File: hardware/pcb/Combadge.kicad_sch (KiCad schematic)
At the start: 12 parts, among them J1 Conn_01x05_Female, U2 ESP32-WROOM-32

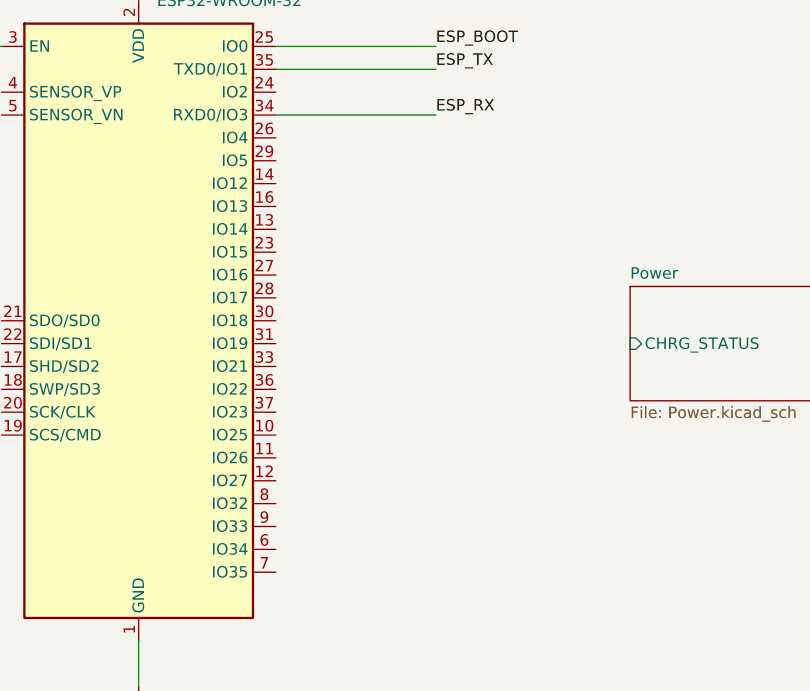
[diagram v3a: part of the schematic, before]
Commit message: Connect I2S devices to ESP32
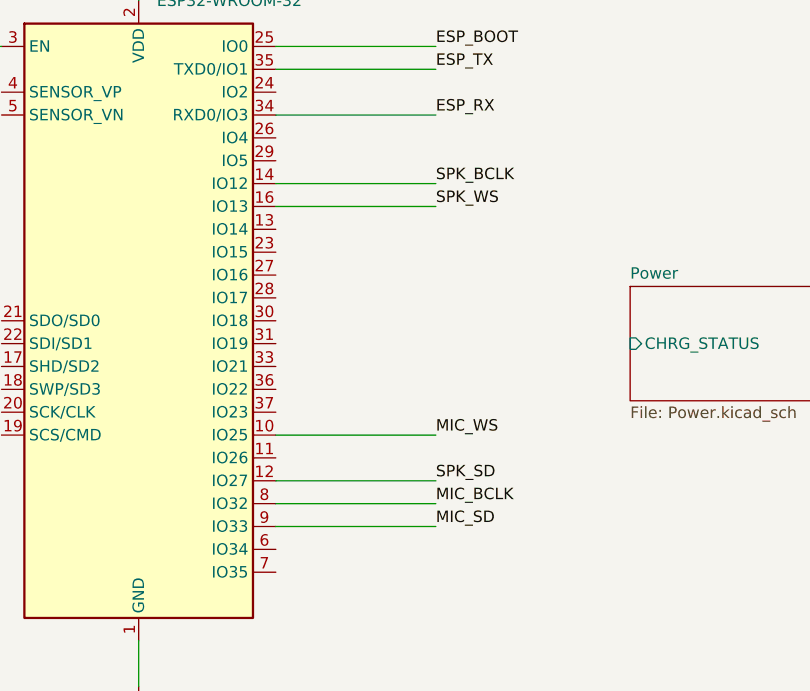
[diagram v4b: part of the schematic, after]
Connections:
- net MIC_BCLK: now also U2.8 (IO32)
- net MIC_SD: now also U2.9 (IO33)
- net MIC_WS: now also U2.10 (IO25)
- net SPK_BCLK: now also U2.14 (IO12)
- net SPK_SD: now also U2.12 (IO27)
- net SPK_WS: now also U2.16 (IO13)
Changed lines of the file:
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@@
+    (stroke (width 0) (type default) (color 0 0 0 0))
+  )
+  (wire (pts (xy 88.9 71.12) (xy 106.68 71.12))
     (stroke (width 0) (type default) (color 0 0 0 0))
   )
@@
     (stroke (width 0) (type default) (color 0 0 0 0))
   )
+  (wire (pts (xy 88.9 109.22) (xy 106.68 109.22))
+    (stroke (width 0) (type default) (color 0 0 0 0))
+  )
   (wire (pts (xy 88.9 63.5) (xy 106.68 63.5))
     (stroke (width 0) (type default) (color 0 0 0 0))
@@
     (stroke (width 0) (type default) (color 0 0 0 0))
   )
+  (wire (pts (xy 88.9 104.14) (xy 106.68 104.14))
+    (stroke (width 0) (type default) (color 0 0 0 0))
+  )
   (wire (pts (xy 20.32 181.61) (xy 34.29 181.61))
     (stroke (width 0) (type default) (color 0 0 0 0))
@@
     (stroke (width 0) (type default) (color 0 0 0 0))
   )
+  (wire (pts (xy 88.9 106.68) (xy 106.68 106.68))
+    (stroke (width 0) (type default) (color 0 0 0 0))
+  )
+  (wire (pts (xy 88.9 99.06) (xy 106.68 99.06))
+    (stroke (width 0) (type default) (color 0 0 0 0))
+  )
   (wire (pts (xy 77.47 31.75) (xy 73.66 31.75))
     (stroke (width 0) (type default) (color 0 0 0 0))
@@
     (stroke (width 0) (type default) (color 0 0 0 0))
   )
+  (wire (pts (xy 88.9 73.66) (xy 106.68 73.66))
+    (stroke (width 0) (type default) (color 0 0 0 0))
+  )
   (text "No clip gain mode" (at 261.62 110.49 0)
     (effects (font (size 1.27 1.27)) (justify left bottom))
@@
     (effects (font (size 1.27 1.27)) (justify left bottom))
   )
+  (label "SPK_BCLK" (at 106.68 71.12 0)
+    (effects (font (size 1.27 1.27)) (justify left bottom))
+  )
   (label "SPK_EN" (at 212.09 92.71 0)
     (effects (font (size 1.27 1.27)) (justify left bottom))
@@
     (effects (font (size 1.27 1.27)) (justify left bottom))
   )
+  (label "SPK_WS" (at 106.68 73.66 0)
+    (effects (font (size 1.27 1.27)) (justify left bottom))
+  )
+  (label "MIC_BCLK" (at 106.68 106.68 0)
+    (effects (font (size 1.27 1.27)) (justify left bottom))
+  )
   (label "ESP_TX" (at 106.68 58.42 0)
     (effects (font (size 1.27 1.27)) (justify left bottom))
   )
+  (label "MIC_SD" (at 106.68 109.22 0)
+    (effects (font (size 1.27 1.27)) (justify left bottom))
+  )
+  (label "MIC_WS" (at 106.68 99.06 0)
+    (effects (font (size 1.27 1.27)) (justify left bottom))
+  )
   (label "SPK_WS" (at 264.16 90.17 0)
     (effects (font (size 1.27 1.27)) (justify left bottom))
   )
+  (label "SPK_SD" (at 106.68 104.14 0)
+    (effects (font (size 1.27 1.27)) (justify left bottom))
+  )

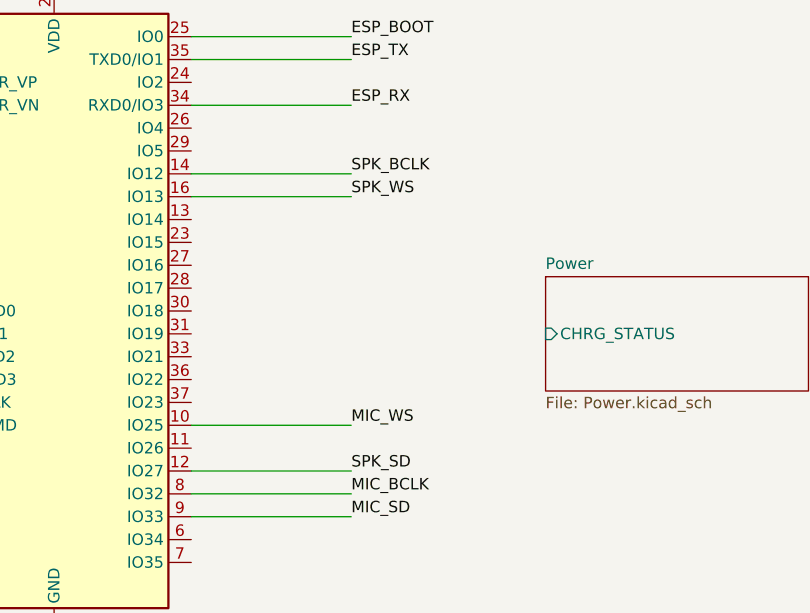
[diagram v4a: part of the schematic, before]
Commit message: Make ancillary ESP32 connections
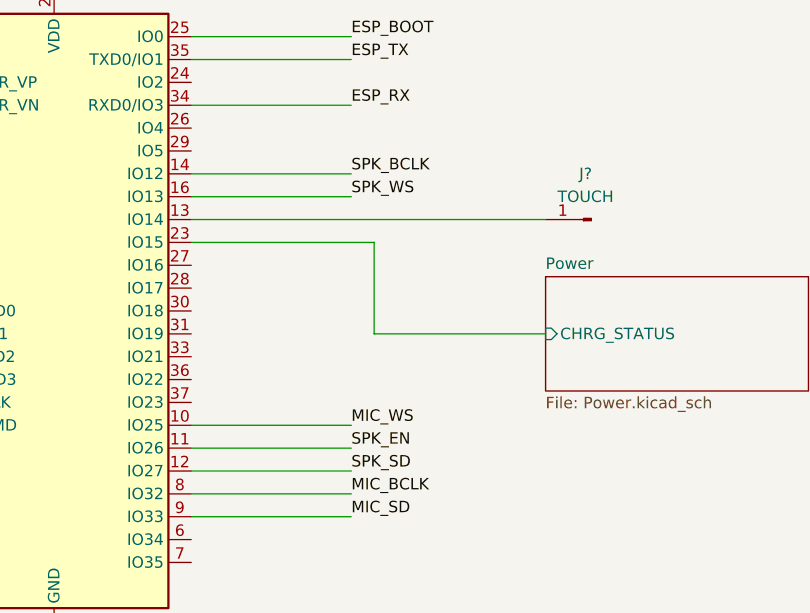
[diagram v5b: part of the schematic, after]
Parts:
- added J?: TOUCH, symbol Connector:Conn_01x01_Male
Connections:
- net Power/CHRG_STATUS: now also U2.23 (IO15)
- net SPK_EN: now also U2.11 (IO26)
- net at U2.13 (IO14): now also J?.1 (Pin_1)
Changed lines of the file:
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@@
+    (stroke (width 0) (type default) (color 0 0 0 0))
+  )
+  (wire (pts (xy 109.22 88.9) (xy 128.27 88.9))
     (stroke (width 0) (type default) (color 0 0 0 0))
   )
@@
     (stroke (width 0) (type default) (color 0 0 0 0))
   )
+  (wire (pts (xy 109.22 78.74) (xy 109.22 88.9))
+    (stroke (width 0) (type default) (color 0 0 0 0))
+  )
   (wire (pts (xy 220.98 87.63) (xy 228.6 87.63))
     (stroke (width 0) (type default) (color 0 0 0 0))
@@
     (stroke (width 0) (type default) (color 0 0 0 0))
   )
+  (wire (pts (xy 88.9 101.6) (xy 106.68 101.6))
+    (stroke (width 0) (type default) (color 0 0 0 0))
+  )
   (wire (pts (xy 248.92 29.21) (xy 256.54 29.21))
     (stroke (width 0) (type default) (color 0 0 0 0))
@@
     (stroke (width 0) (type default) (color 0 0 0 0))
   )
+  (wire (pts (xy 88.9 78.74) (xy 109.22 78.74))
+    (stroke (width 0) (type default) (color 0 0 0 0))
+  )
   (wire (pts (xy 36.83 36.83) (xy 44.45 36.83))
     (stroke (width 0) (type default) (color 0 0 0 0))
@@
     (stroke (width 0) (type default) (color 0 0 0 0))
   )
+  (wire (pts (xy 88.9 76.2) (xy 128.27 76.2))
+    (stroke (width 0) (type default) (color 0 0 0 0))
+  )
   (wire (pts (xy 205.74 34.29) (xy 213.36 34.29))
     (stroke (width 0) (type default) (color 0 0 0 0))
@@
   )
   (label "ESP_RX" (at 106.68 63.5 0)
+    (effects (font (size 1.27 1.27)) (justify left bottom))
+  )
+  (label "SPK_EN" (at 106.68 101.6 0)
     (effects (font (size 1.27 1.27)) (justify left bottom))
   )
@@
     (pin "2")
   )
+  (symbol (lib_id "Connector:Conn_01x01_Male") (at 133.35 76.2 180) (unit 1)
+    (in_bom yes) (on_board yes) (fields_autoplaced)
+    (property "Reference" "J?" (id 0) (at 132.715 71.12 0))
+    (property "Value" "TOUCH" (id 1) (at 132.715 73.66 0))
+    (property "Footprint" "" (id 2) (at 133.35 76.2 0)
+      (effects (font (size 1.27 1.27)) hide)
+    )
+    (property "Datasheet" "~" (id 3) (at 133.35 76.2 0)
+      (effects (font (size 1.27 1.27)) hide)
+    )
+    (pin "1")
+  )
   (symbol (lib_id "power:+3.3V") (at 30.48 189.23 180) (unit 1)
     (in_bom yes) (on_board yes) (fields_autoplaced)
@@
       (reference "J2") (unit 1) (value "USB_B_Micro") (footprint "")
     )
+    (path "/a6e5c9c8-cb7b-408f-828d-ae46f4af3d38"
+      (reference "J?") (unit 1) (value "TOUCH") (footprint "")
+    )
     (path "/7c65d4b9-482c-4a7d-9365-126ab5b66d1e"

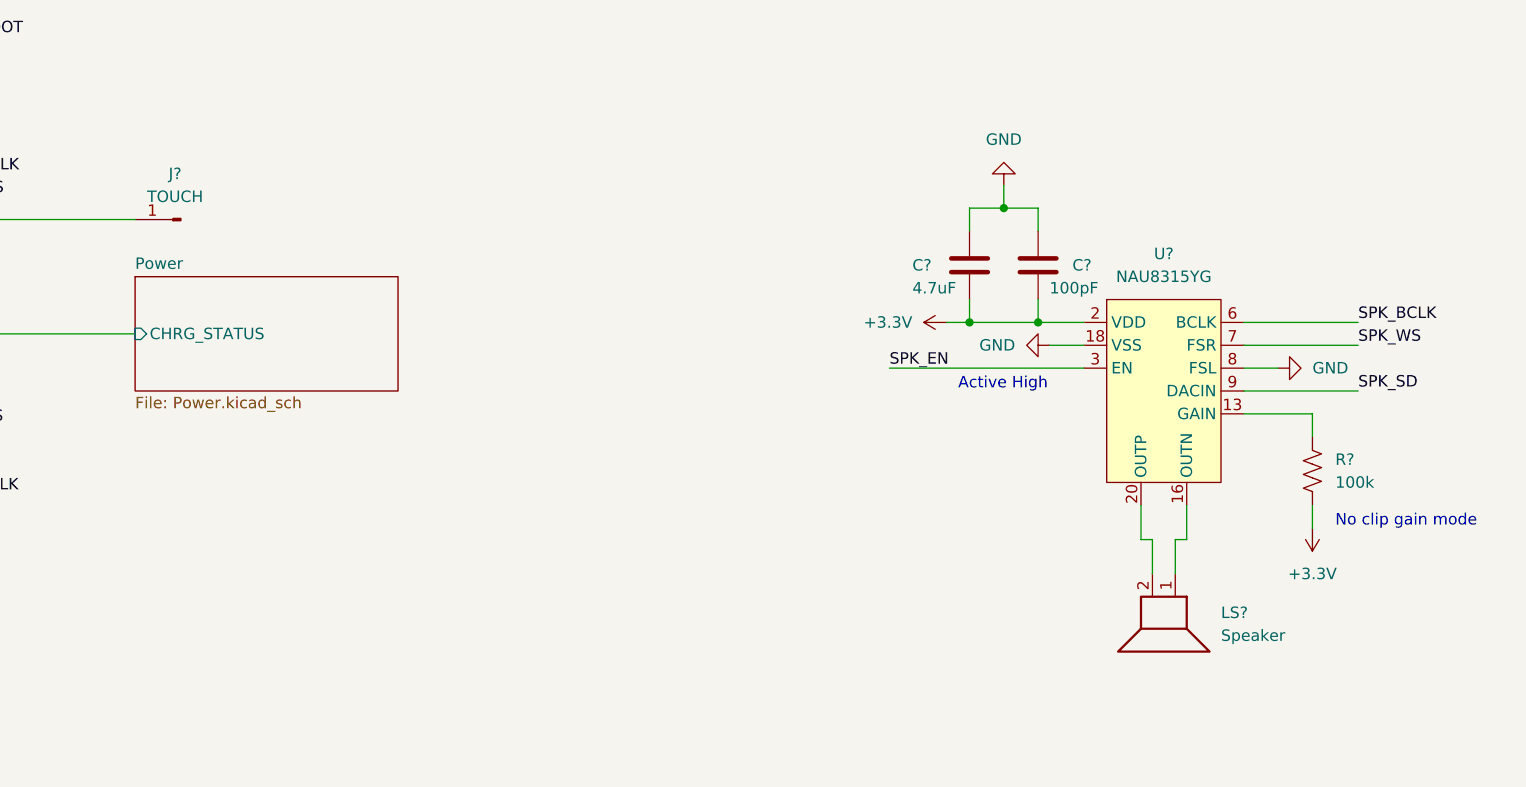
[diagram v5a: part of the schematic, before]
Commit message: Add schematic titles
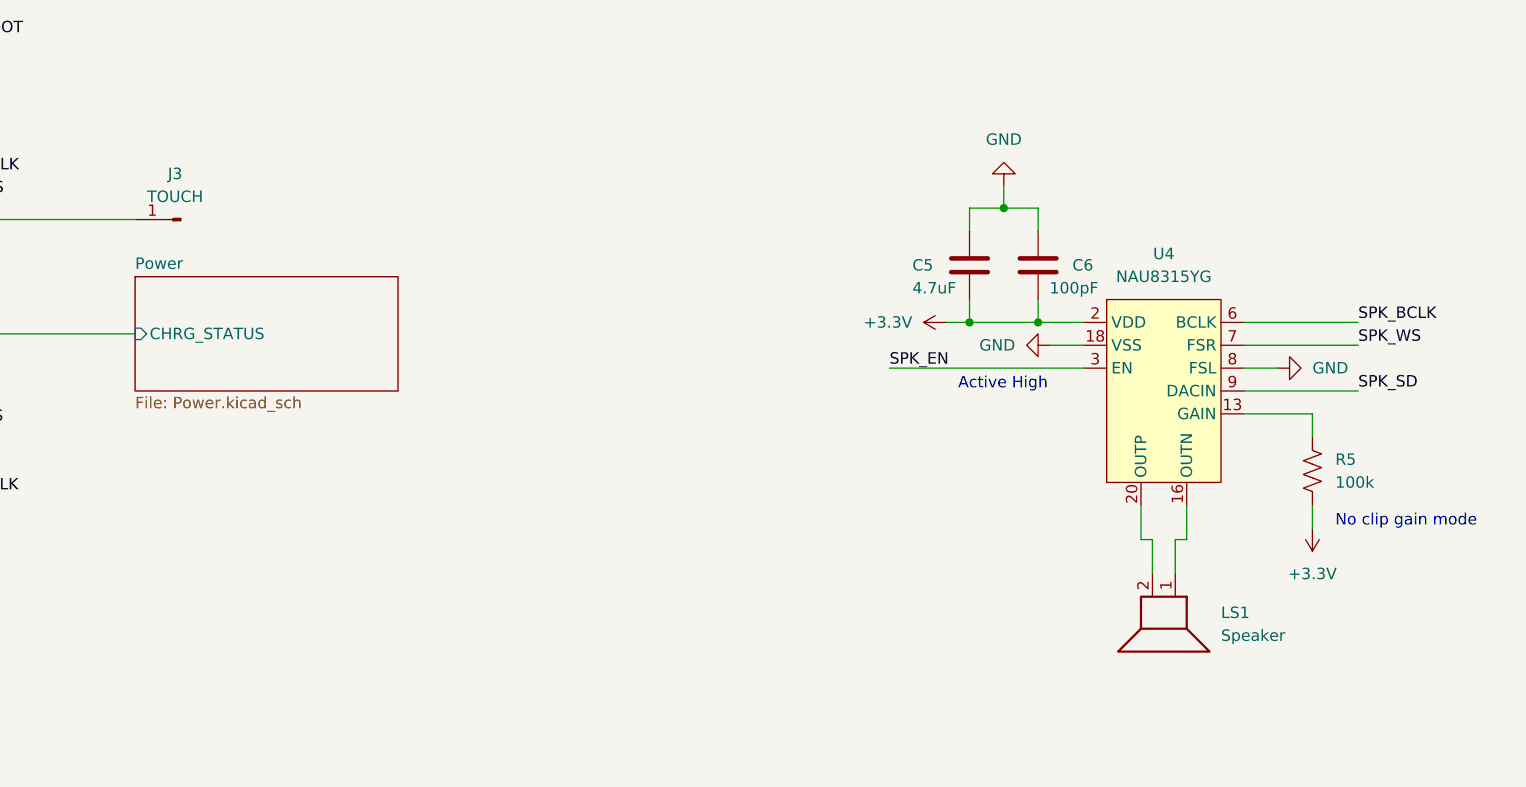
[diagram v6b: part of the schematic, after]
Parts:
- gave numbers to parts that had none: 6
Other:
- title: (none) -> Combadge
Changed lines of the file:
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@@
 (kicad_sch (version 20211123) (generator eeschema)
   (paper "A4")
+  (title_block
+    (title "Combadge")
+    (rev "1")
+  )
   (junction (at 44.45 36.83) (diameter 0) (color 0 0 0 0)
   )
@@
   (symbol (lib_id "power:GND") (at 229.87 90.17 270) (unit 1)
     (in_bom yes) (on_board yes) (fields_autoplaced)
-    (property "Reference" "#PWR?" (id 0) (at 223.52 90.17 0)
+    (property "Reference" "#PWR0114" (id 0) (at 223.52 90.17 0)
       (effects (font (size 1.27 1.27)) hide)
     )
@@
   (symbol (lib_id "power:+3.3V") (at 259.08 110.49 180) (unit 1)
     (in_bom yes) (on_board yes) (fields_autoplaced)
-    (property "Reference" "#PWR?" (id 0) (at 259.08 106.68 0)
+    (property "Reference" "#PWR0117" (id 0) (at 259.08 106.68 0)
       (effects (font (size 1.27 1.27)) hide)
     )
@@
   (symbol (lib_id "power:GND") (at 255.27 92.71 90) (unit 1)
     (in_bom yes) (on_board yes) (fields_autoplaced)
-    (property "Reference" "#PWR?" (id 0) (at 261.62 92.71 0)
+    (property "Reference" "#PWR0115" (id 0) (at 261.62 92.71 0)
       (effects (font (size 1.27 1.27)) hide)
     )
@@
   (symbol (lib_id "Device:C") (at 220.98 81.28 0) (unit 1)
     (in_bom yes) (on_board yes)
-    (property "Reference" "C?" (id 0) (at 214.63 81.28 0)
+    (property "Reference" "C5" (id 0) (at 214.63 81.28 0)
       (effects (font (size 1.27 1.27)) (justify left))
     )
@@
   (symbol (lib_id "Device:R_US") (at 259.08 104.14 0) (unit 1)
     (in_bom yes) (on_board yes) (fields_autoplaced)
-    (property "Reference" "R?" (id 0) (at 261.62 102.8699 0)
+    (property "Reference" "R5" (id 0) (at 261.62 102.8699 0)
       (effects (font (size 1.27 1.27)) (justify left))
     )
@@
   (symbol (lib_id "power:GND") (at 224.79 72.39 180) (unit 1)
     (in_bom yes) (on_board yes) (fields_autoplaced)
-    (property "Reference" "#PWR?" (id 0) (at 224.79 66.04 0)
+    (property "Reference" "#PWR0118" (id 0) (at 224.79 66.04 0)
       (effects (font (size 1.27 1.27)) hide)
     )
@@
   (symbol (lib_id "Device:Speaker") (at 243.84 120.65 270) (unit 1)
     (in_bom yes) (on_board yes) (fields_autoplaced)
-    (property "Reference" "LS?" (id 0) (at 248.92 119.8879 90)
+    (property "Reference" "LS1" (id 0) (at 248.92 119.8879 90)
       (effects (font (size 1.27 1.27)) (justify left))
     )
@@
   (symbol (lib_id "power:+3.3V") (at 218.44 87.63 90) (unit 1)
     (in_bom yes) (on_board yes) (fields_autoplaced)
-    (property "Reference" "#PWR?" (id 0) (at 222.25 87.63 0)
+    (property "Reference" "#PWR0116" (id 0) (at 222.25 87.63 0)
       (effects (font (size 1.27 1.27)) hide)
     )
@@
   (symbol (lib_id "Nuvoton:NAU8315YG") (at 242.57 82.55 0) (unit 1)
     (in_bom yes) (on_board yes) (fields_autoplaced)
-    (property "Reference" "U?" (id 0) (at 242.57 80.01 0))
+    (property "Reference" "U4" (id 0) (at 242.57 80.01 0))
     (property "Value" "NAU8315YG" (id 1) (at 242.57 82.55 0))
     (property "Footprint" "CustomQFN:QFN-20-1EP_4x4mm_P0.5mm_EP2x2mm" (id 2) (at 242.57 77.47 0)
@@
   (symbol (lib_id "Connector:Conn_01x01_Male") (at 133.35 76.2 180) (unit 1)
     (in_bom yes) (on_board yes) (fields_autoplaced)
-    (property "Reference" "J?" (id 0) (at 132.715 71.12 0))
+    (property "Reference" "J3" (id 0) (at 132.715 71.12 0))
     (property "Value" "TOUCH" (id 1) (at 132.715 73.66 0))
     (property "Footprint" "" (id 2) (at 133.35 76.2 0)
@@
   (symbol (lib_id "Device:C") (at 228.6 81.28 0) (unit 1)
     (in_bom yes) (on_board yes)
-    (property "Reference" "C?" (id 0) (at 232.41 81.28 0)
+    (property "Reference" "C6" (id 0) (at 232.41 81.28 0)
       (effects (font (size 1.27 1.27)) (justify left))
     )
@@
   (symbol (lib_id "power:+3.3V") (at 205.74 34.29 90) (unit 1)
     (in_bom yes) (on_board yes) (fields_autoplaced)
-    (property "Reference" "#PWR?" (id 0) (at 209.55 34.29 0)
+    (property "Reference" "#PWR0119" (id 0) (at 209.55 34.29 0)
       (effects (font (size 1.27 1.27)) hide)
     )
@@
     )
     (path "/1b5d8123-fe2f-4957-86ba-aece6f7812d0"
-      (reference "#PWR?") (unit 1) (value "GND") (footprint "")
+      (reference "#PWR0114") (unit 1) (value "GND") (footprint "")
+    )
+    (path "/3ee41b2d-f3da-4dcf-95f9-4d2f53bf980d"
+      (reference "#PWR0115") (unit 1) (value "GND") (footprint "")
+    )
+    (path "/89af64ba-41d6-4971-ace0-48f71957e655"
+      (reference "#PWR0116") (unit 1) (value "+3.3V") (footprint "")
     )
     (path "/1f197de7-8f64-4aef-b52a-422fae11f49e"
-      (reference "#PWR?") (unit 1) (value "+3.3V") (footprint "")
-    )
-    (path "/3ee41b2d-f3da-4dcf-95f9-4d2f53bf980d"
-      (reference "#PWR?") (unit 1) (value "GND") (footprint "")
+      (reference "#PWR0117") (unit 1) (value "+3.3V") (footprint "")
     )
     (path "/71ff710a-c937-4bbd-a8e2-13fcf45b7663"
-      (reference "#PWR?") (unit 1) (value "GND") (footprint "")
-    )
-    (path "/89af64ba-41d6-4971-ace0-48f71957e655"
-      (reference "#PWR?") (unit 1) (value "+3.3V") (footprint "")
+      (reference "#PWR0118") (unit 1) (value "GND") (footprint "")
     )
     (path "/e58f6e5e-a452-440f-af9f-6aee729c4980"
-      (reference "#PWR?") (unit 1) (value "+3.3V") (footprint "")
+      (reference "#PWR0119") (unit 1) (value "+3.3V") (footprint "")
     )
     (path "/522738f4-f6b2-4897-a079-07da122bd152/54fa1821-1962-473c-8470-e88a1b27fa8c"
@@
     )
     (path "/45675717-f492-4f4f-a167-18356673890d"
-      (reference "C?") (unit 1) (value "4.7uF") (footprint "")
+      (reference "C5") (unit 1) (value "4.7uF") (footprint "")
     )
     (path "/c9c68790-db29-4468-810c-d11a4b68e482"
-      (reference "C?") (unit 1) (value "100pF") (footprint "")
+      (reference "C6") (unit 1) (value "100pF") (footprint "")
     )
     (path "/522738f4-f6b2-4897-a079-07da122bd152/90b83734-9b32-498c-90f9-3d6e745143bf"
@@
     )
     (path "/a6e5c9c8-cb7b-408f-828d-ae46f4af3d38"
-      (reference "J?") (unit 1) (value "TOUCH") (footprint "")
+      (reference "J3") (unit 1) (value "TOUCH") (footprint "")
     )
     (path "/7c65d4b9-482c-4a7d-9365-126ab5b66d1e"
-      (reference "LS?") (unit 1) (value "Speaker") (footprint "")
+      (reference "LS1") (unit 1) (value "Speaker") (footprint "")
     )
     (path "/6692667a-23d9-4d51-a0f9-87ae21b84031"
@@
     )
     (path "/65ecb276-9d69-4f1a-bd2e-69221f373bf0"
-      (reference "R?") (unit 1) (value "100k") (footprint "")
+      (reference "R5") (unit 1) (value "100k") (footprint "")
     )
     (path "/522738f4-f6b2-4897-a079-07da122bd152/bd72950c-6810-4eec-8819-388bfc93ab04"
@@
     )
     (path "/a3e9f322-b8d4-47c2-ad48-edf4cfe76ba5"
-      (reference "U?") (unit 1) (value "NAU8315YG") (footprint "CustomQFN:QFN-20-1EP_4x4mm_P0.5mm_EP2x2mm")
-    )
-  )
+      (reference "U4") (unit 1) (value "NAU8315YG") (footprint "CustomQFN:QFN-20-1EP_4x4mm_P0.5mm_EP2x2mm")
+    )
+  )
